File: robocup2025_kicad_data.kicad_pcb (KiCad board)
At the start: 4 copper layers, 88.1 x 96.9 mm, 19 parts, among them M7 Motor_Servo, U2 ESP32-DEVKITC-32E

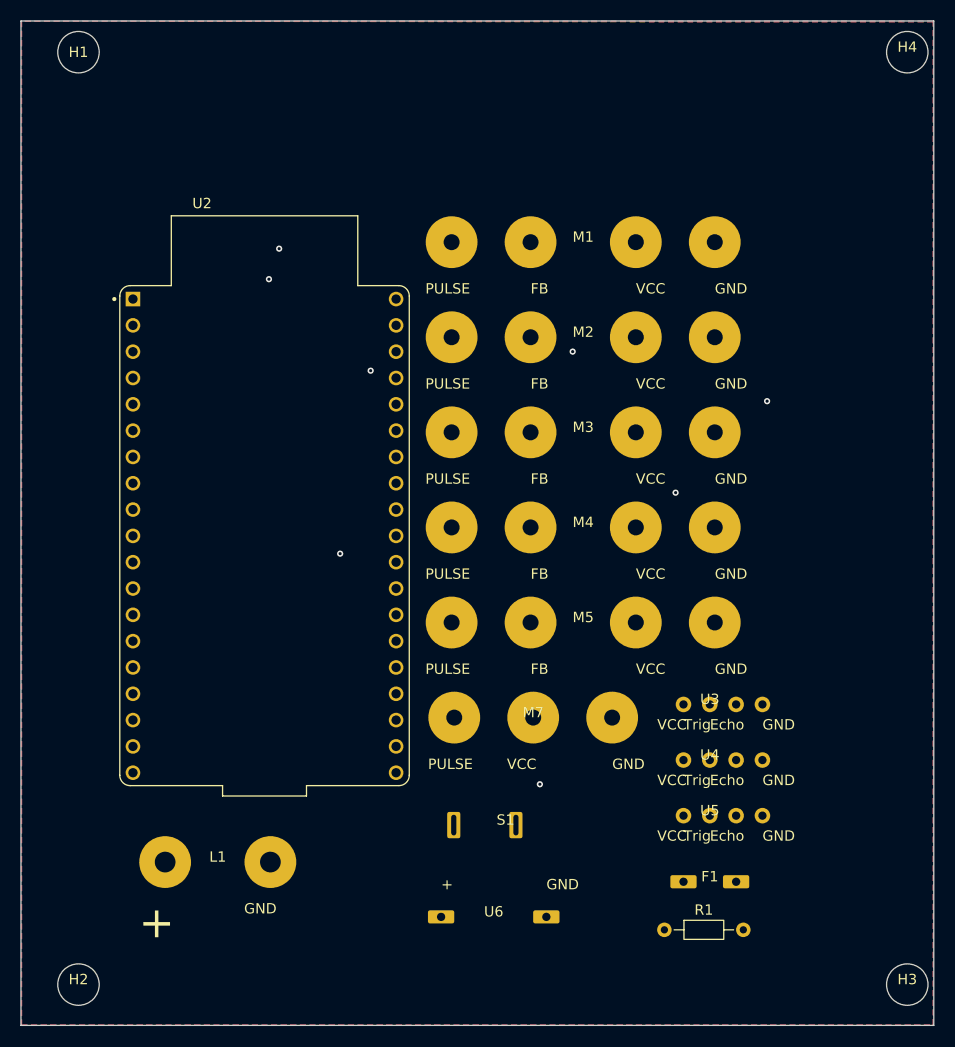
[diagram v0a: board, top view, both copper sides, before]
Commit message: removed all lines and vias
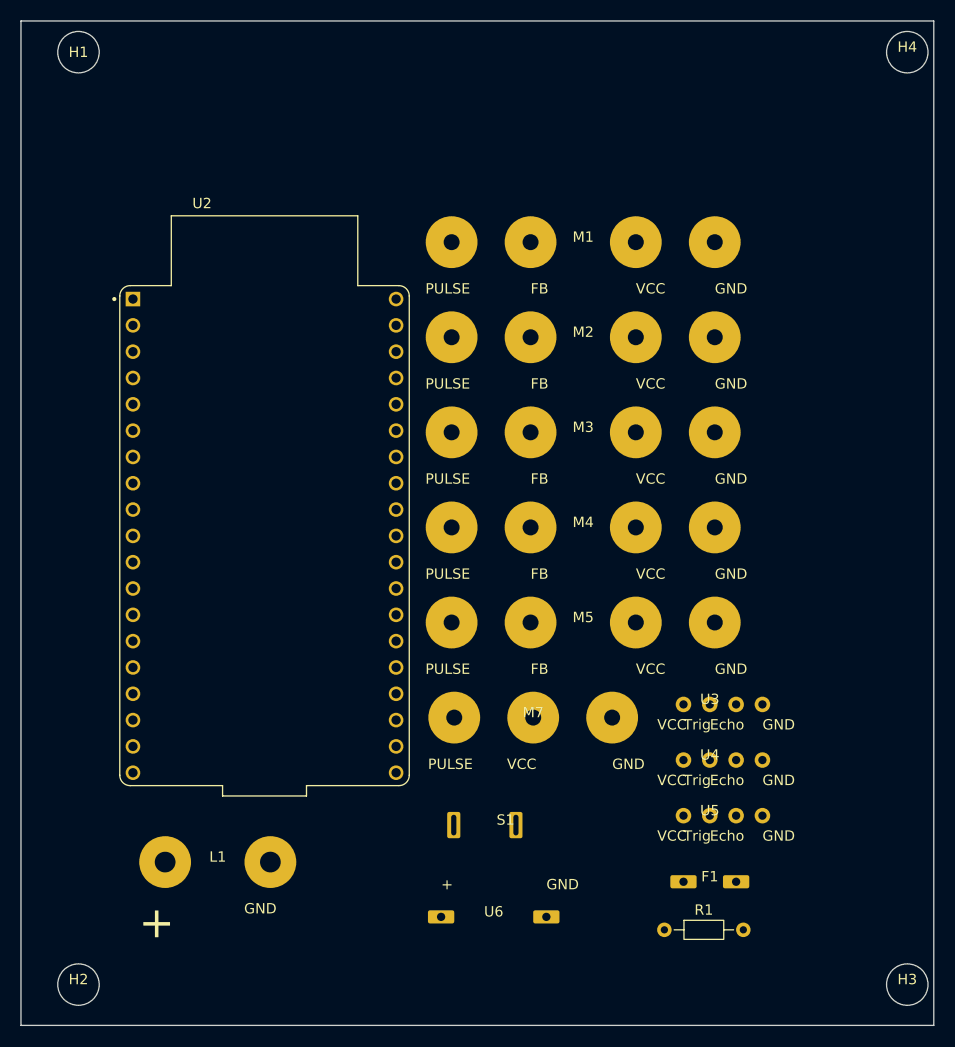
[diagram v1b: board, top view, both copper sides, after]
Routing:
- net ESP32_3.3: track 121.8 -> 0.00 mm, vias 2 -> 0
- net ultrasonic_echo2: track 75.8 -> 0.00 mm, vias 1 -> 0
- net ESP32_21: track 72.9 -> 0.00 mm
- net arm_feedback: track 72.3 -> 0.00 mm, vias 1 -> 0
- net ultrasonic_echo3: track 70.2 -> 0.00 mm
- net ultrasonic_trig3: track 68.3 -> 0.00 mm
- net tyre_pulse_1: track 63.4 -> 0.00 mm, vias 1 -> 0
- net Net-(L1-+): track 60.9 -> 0.00 mm
- net ultrasonic_trig2: track 60.4 -> 0.00 mm, vias 1 -> 0
- net arm_wire_SIG: track 58.5 -> 0.00 mm, vias 1 -> 0
- net tyre_pulse_2: track 55.5 -> 0.00 mm, vias 1 -> 0
- net ultrasonic_echo1: track 44.4 -> 0.00 mm
- net ultrasonic_trig1: track 40.2 -> 0.00 mm
- net tyre_pulse_3: track 31.9 -> 0.00 mm
- net tyre_pulse_4: track 8.12 -> 0.00 mm
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- removed copper zone on F.Cu, net GND
- removed copper zone on B.Cu, net LiPo+

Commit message: replaced all the items on pcb
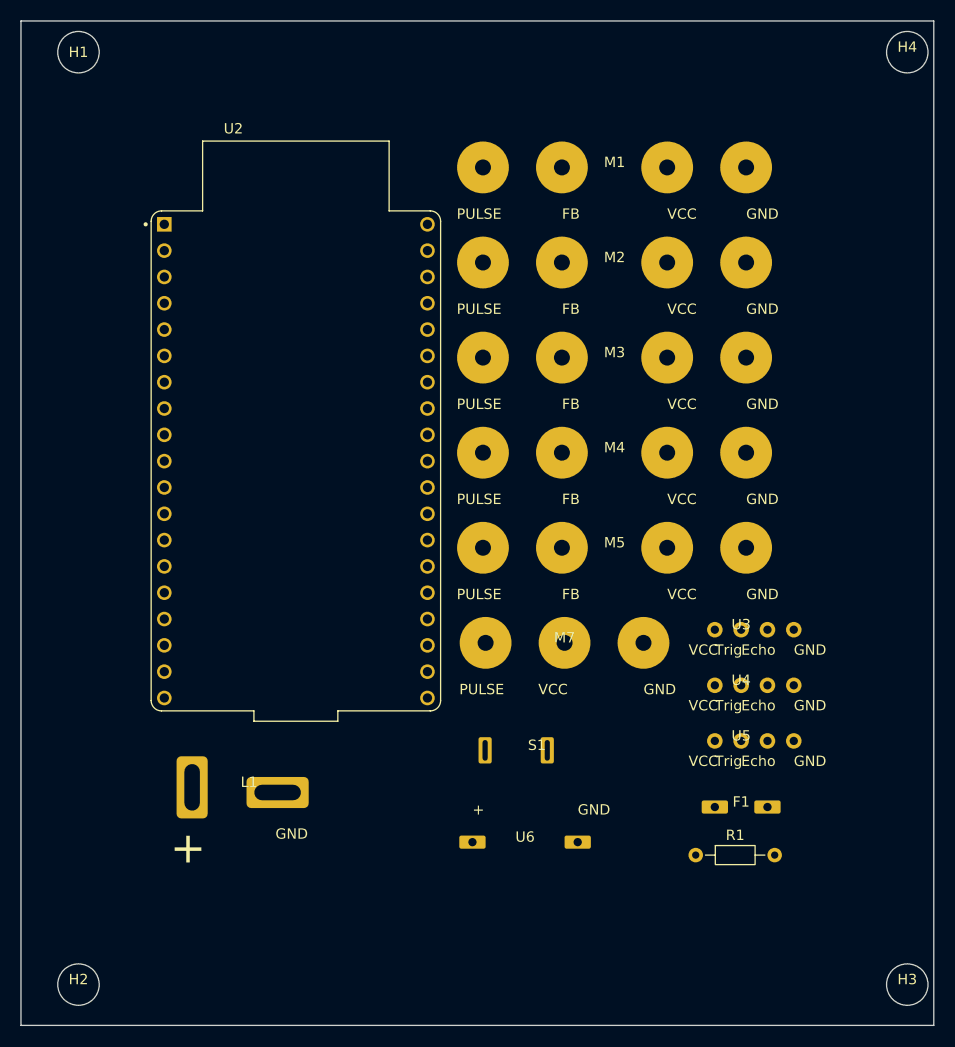
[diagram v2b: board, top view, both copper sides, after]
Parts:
- moved L1 7.82 mm to (125.3, 111.0)
- moved M2 7.82 mm to (160.5, 60.3)
- moved F1 7.82 mm to (172.8, 112.9)
- moved M1 7.82 mm to (160.5, 51.1)
- moved M3 7.82 mm to (160.5, 69.5)
- moved M4 7.82 mm to (160.5, 78.7)
- moved M5 7.82 mm to (160.5, 87.8)
- moved S1 7.82 mm to (153.1, 107.4)
- moved U3 7.82 mm to (172.8, 95.7)
- moved U4 7.82 mm to (172.8, 101.1)
- moved U5 7.82 mm to (172.8, 106.5)
- moved U2 7.82 mm to (129.8, 79.5)
- moved M7 7.82 mm to (155.7, 97.0)
- moved R1 7.82 mm to (168.4, 117.5)
- moved U6 7.82 mm to (151.9, 116.2)

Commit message: filled all the f.cu and b.cu
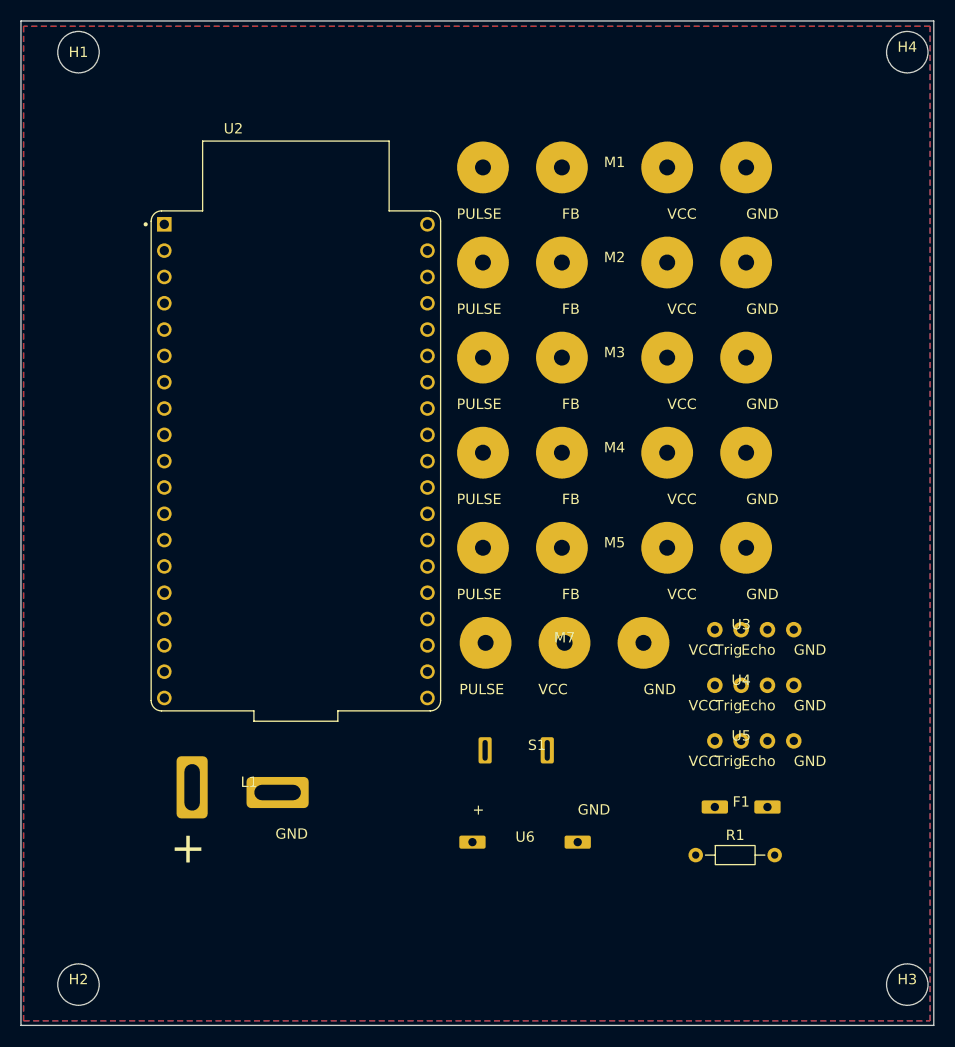
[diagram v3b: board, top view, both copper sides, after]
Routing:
- added copper zone on F.Cu, net GND
- added copper zone on B.Cu, net LiPo+
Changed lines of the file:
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@@
 		(layer "Edge.Cuts")
+	)
+	(zone
+		(net 2)
+		(net_name "GND")
+		(layer "F.Cu")
+		(hatch edge 0.5)
+		(connect_pads
+			(clearance 0.5)
+		)
+		(min_thickness 0.25)
+		(filled_areas_thickness no)
+		(fill yes
+			(thermal_gap 0.5)
+			(thermal_bridge_width 0.5)
+		)
+		(polygon
+			(pts
+				(xy 103.5 37.5) (xy 103.5 133.5) (xy 191 133.5) (xy 191 37.5)
+			)
+		)
+	)
+	(zone
+		(net 1)
+		(net_name "LiPo+")
+		(layer "B.Cu")
+		(hatch edge 0.5)
+		(priority 1)
+		(connect_pads
+			(clearance 0.5)
+		)
+		(min_thickness 0.25)
+		(filled_areas_thickness no)
+		(fill yes
+			(thermal_gap 0.5)
+			(thermal_bridge_width 0.5)
+		)
+		(polygon
+			(pts
+				(xy 103.5 37.5) (xy 103.5 133.5) (xy 191 133.5) (xy 191 37.5)
+			)
+		)
 	)
 	(embedded_fonts no)

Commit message: routed all parts
DRC passing
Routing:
- net ESP32_3.3: track 0.00 -> 103.0 mm
- net tyre_pulse_1: track 0.00 -> 84.4 mm, vias 0 -> 1
- net arm_feedback: track 0.00 -> 83.2 mm, vias 0 -> 1
- net ESP32_21: track 0.00 -> 75.4 mm, vias 0 -> 1
- net ultrasonic_trig3: track 0.00 -> 75.3 mm, vias 0 -> 1
- net ultrasonic_echo3: track 0.00 -> 68.5 mm
- net ultrasonic_echo2: track 0.00 -> 67.9 mm, vias 0 -> 1
- net ultrasonic_trig2: track 0.00 -> 65.4 mm, vias 0 -> 1
- net tyre_pulse_2: track 0.00 -> 64.2 mm
- net arm_wire_SIG: track 0.00 -> 64.0 mm, vias 0 -> 1
- net Net-(L1-+): track 0.00 -> 59.1 mm
- net ultrasonic_echo1: track 0.00 -> 46.5 mm
- net ultrasonic_trig1: track 0.00 -> 45.9 mm
- net tyre_pulse_3: track 0.00 -> 30.1 mm
- net tyre_pulse_4: track 0.00 -> 8.12 mm
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
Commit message: fixed size of the button
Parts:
- moved S1 0.12 mm to (153.0, 107.5)

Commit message: clean
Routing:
- net ESP32_3.3: track 103.0 -> 0.00 mm
- net tyre_pulse_1: track 84.4 -> 0.00 mm, vias 1 -> 0
- net arm_feedback: track 83.2 -> 0.00 mm, vias 1 -> 0
- net ESP32_21: track 75.4 -> 0.00 mm, vias 1 -> 0
- net ultrasonic_trig3: track 75.3 -> 0.00 mm, vias 1 -> 0
- net ultrasonic_echo3: track 68.5 -> 0.00 mm
- net ultrasonic_echo2: track 67.9 -> 0.00 mm, vias 1 -> 0
- net ultrasonic_trig2: track 65.4 -> 0.00 mm, vias 1 -> 0
- net tyre_pulse_2: track 64.2 -> 0.00 mm
- net arm_wire_SIG: track 64.0 -> 0.00 mm, vias 1 -> 0
- net Net-(L1-+): track 59.1 -> 0.00 mm
- net ultrasonic_echo1: track 46.5 -> 0.00 mm
- net ultrasonic_trig1: track 45.9 -> 0.00 mm
- net tyre_pulse_3: track 30.1 -> 0.00 mm
- net tyre_pulse_4: track 8.12 -> 0.00 mm
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- removed copper zone on F.Cu, net GND
- removed copper zone on B.Cu, net LiPo+

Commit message: Lipo and GND
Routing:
- added copper zone on F.Cu, net GND
- added copper zone on B.Cu, net LiPo+
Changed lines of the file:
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@@
 		(layer "Edge.Cuts")
+	)
+	(zone
+		(net 2)
+		(net_name "GND")
+		(layer "F.Cu")
+		(hatch edge 0.5)
+		(connect_pads
+			(clearance 0.5)
+		)
+		(min_thickness 0.25)
+		(filled_areas_thickness no)
+		(fill yes
+			(thermal_gap 0.5)
+			(thermal_bridge_width 0.5)
+		)
+		(polygon
+			(pts
+				(xy 103.5 37.5) (xy 191 37.5) (xy 191 133.5) (xy 103.5 133.5)
+			)
+		)
+	)
+	(zone
+		(net 1)
+		(net_name "LiPo+")
+		(layer "B.Cu")
+		(hatch edge 0.5)
+		(priority 1)
+		(connect_pads
+			(clearance 0.5)
+		)
+		(min_thickness 0.25)
+		(filled_areas_thickness no)
+		(fill yes
+			(thermal_gap 0.5)
+			(thermal_bridge_width 0.5)
+		)
+		(polygon
+			(pts
+				(xy 103.5 37.5) (xy 191 37.5) (xy 191 133.5) (xy 103.5 133.5)
+			)
+		)
 	)
 	(embedded_fonts no)

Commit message: fixed
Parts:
- moved L1 31.3 mm to (153.2, 125.0)
- moved U6 27.9 mm to (124.4, 111.5)
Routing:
- net ESP32_3.3: track 0.00 -> 141.9 mm, vias 0 -> 1
- net arm_feedback: track 0.00 -> 78.1 mm, vias 0 -> 1
- net ultrasonic_trig1: track 0.00 -> 71.5 mm, vias 0 -> 2
- net tyre_pulse_1: track 0.00 -> 71.2 mm, vias 0 -> 1
- net ultrasonic_echo3: track 0.00 -> 71.1 mm
- net ESP32_21: track 0.00 -> 70.5 mm
- net ultrasonic_trig2: track 0.00 -> 69.5 mm, vias 0 -> 1
- net ultrasonic_trig3: track 0.00 -> 68.0 mm
- net Net-(L1-+): track 0.00 -> 67.3 mm
- net ultrasonic_echo2: track 0.00 -> 66.7 mm, vias 0 -> 1
- net arm_wire_SIG: track 0.00 -> 62.8 mm, vias 0 -> 1
- net tyre_pulse_2: track 0.00 -> 48.0 mm
- net ultrasonic_echo1: track 0.00 -> 44.6 mm
- net tyre_pulse_3: track 0.00 -> 31.9 mm
- net tyre_pulse_4: track 0.00 -> 8.12 mm
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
